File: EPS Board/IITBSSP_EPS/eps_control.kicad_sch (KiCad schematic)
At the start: 0 parts

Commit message: Started EPS Control unit design
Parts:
- added 120R: FerriteBead, symbol Device:FerriteBead
- added C10, C11, C16, C5, C6, C7, C8, C9: 100nF, symbol Device:C
- added C12: 10uF, symbol Device:C
- added C13: 10nF, symbol Device:C
- added C14, C15: 1uF, symbol Device:C
- added C17, C18: 6pF, symbol Device:C
- added J1: USB_B_Micro, symbol Connector:USB_B_Micro
- added R5: 10k, symbol Device:R
- added SW1: SW_SPDT, symbol Switch:SW_SPDT
- added U2: STM32L476VET6, Package_QFP:LQFP-100_14x14mm_P0.5mm, symbol MCU_ST_STM32L4:STM32L476VETx
- added Y1: 32MHz, symbol Device:Crystal_GND24
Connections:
- new net +3.3V: 120R.2, C10.1, C11.1, C12.1, C15.1, C5.1, C6.1, C7.1, C8.1, C9.1, SW1.3 (C), U2.100 (VDD), U2.11 (VDD), U2.22 (VDDA), U2.28 (VDD), U2.50 (VDD), U2.6 (VBAT), U2.75 (VDD)
- new net +3.3VA: 120R.1, C13.1, C14.1, U2.73 (VDDUSB)
- new net BOOT0: R5.2, U2.94 (BOOT0)
- new net GND: C10.2, C11.2, C12.2, C13.2, C14.2, C15.2, C16.2, C17.2, C18.2, C5.2, C6.2, C7.2, C8.2, C9.2, J1.5 (GND), SW1.1 (A), U2.10 (VSS), U2.19 (VSSA), U2.27 (VSS), U2.49 (VSS), U2.74 (VSS), U2.99 (VSS), Y1.2, Y1.4
- new net HSE_IN: C17.1, U2.12 (PH0), Y1.1
- new net HSE_OUT: C18.1, U2.13 (PH1), Y1.3
- new net NRST: C16.1, U2.14 (NRST)
- new net SWCLK: U2.76 (PA14)
- new net SWDIO: U2.72 (PA13)
- new net SW_BOOT0: R5.1, SW1.2 (B)
- new net USB_D+: J1.3 (D+), U2.71 (PA12)
- new net USB_D-: J1.2 (D-), U2.70 (PA11)
- new net VBUS: J1.1 (VBUS)
- no-connect marks 0 -> 2
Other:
- note added: "Crystal Circuitry"
- note added: "Load Capacitance = (8-5)*2 = 6pF [8pF (Datasheet) - Stray Capacitance (approx 5pF)]*2"
- note added: "NOTE: VBAT should be tied to external battery or RTC for now have connected with VDD"
- note added: "USB Circuitry"
- company: (none) -> IIT Bombay Student Satellite Program
- title: (none) -> EPS Control Unit

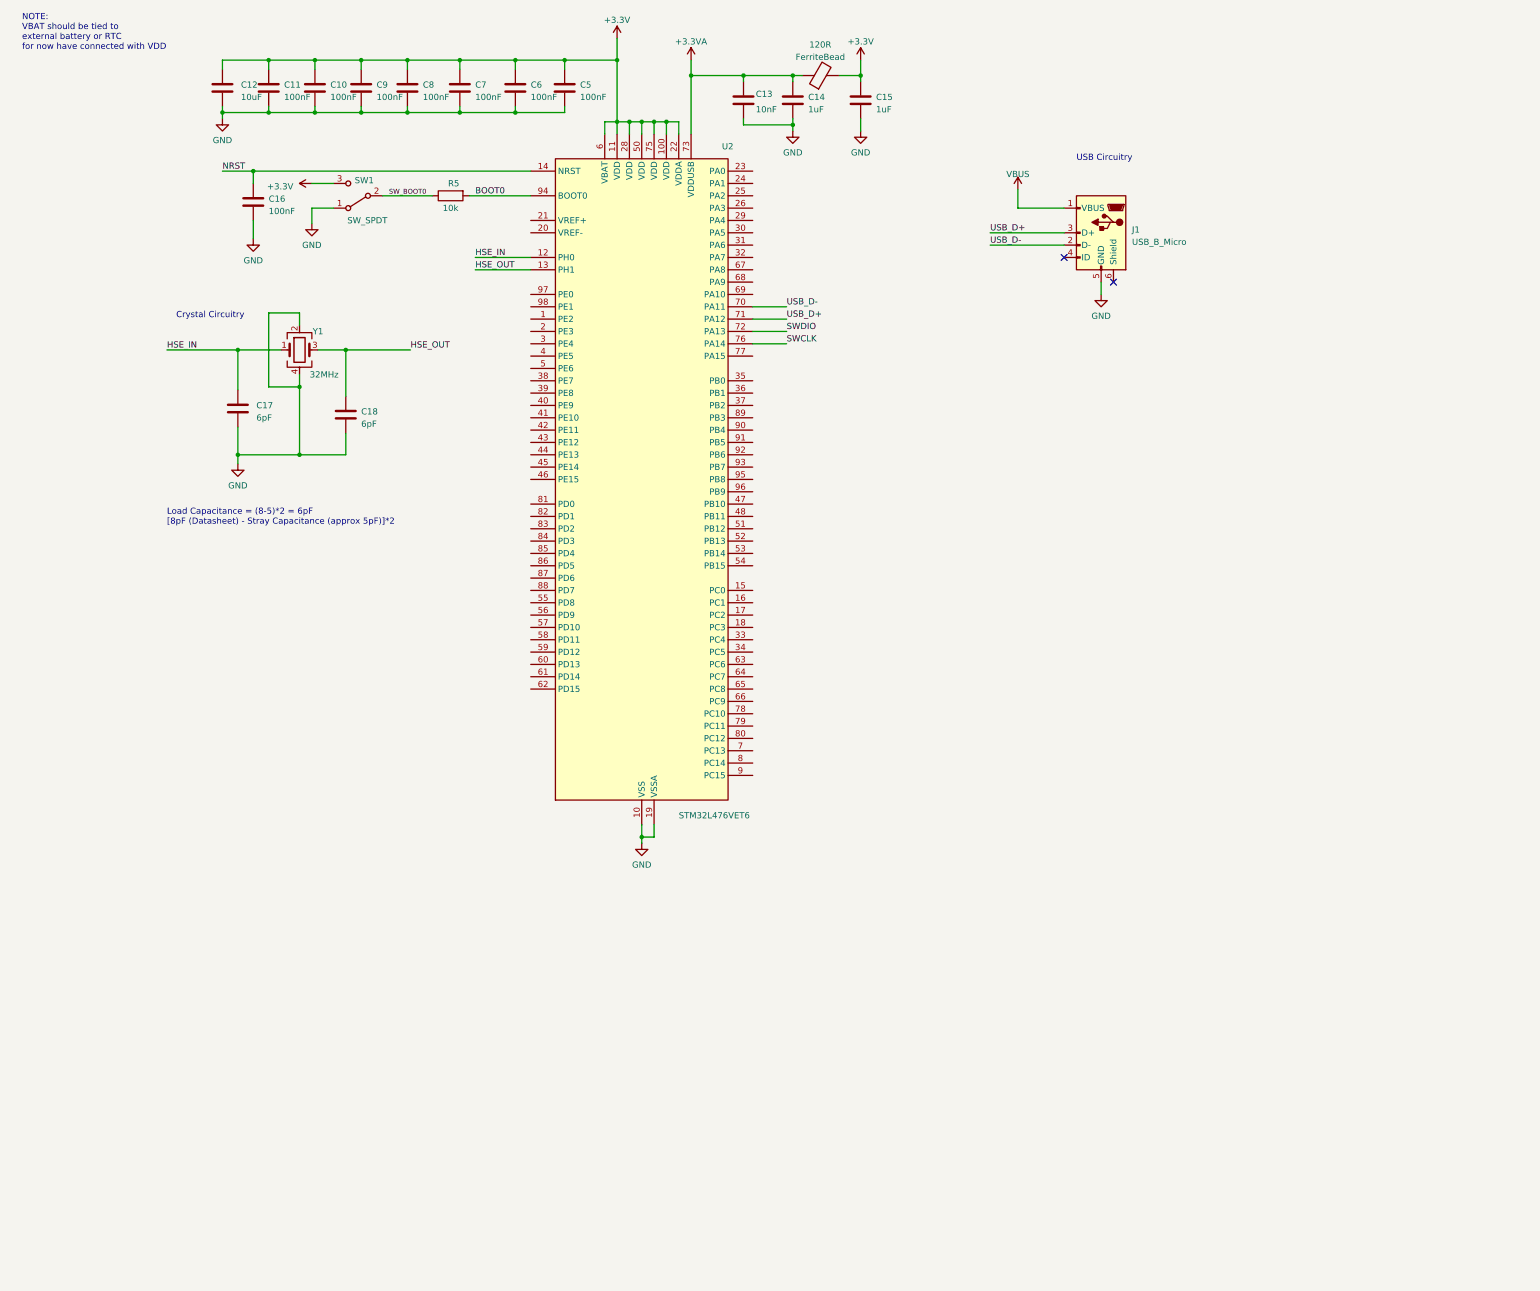
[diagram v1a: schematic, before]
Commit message: EPS Control Unit Dev and Final Schematic designed
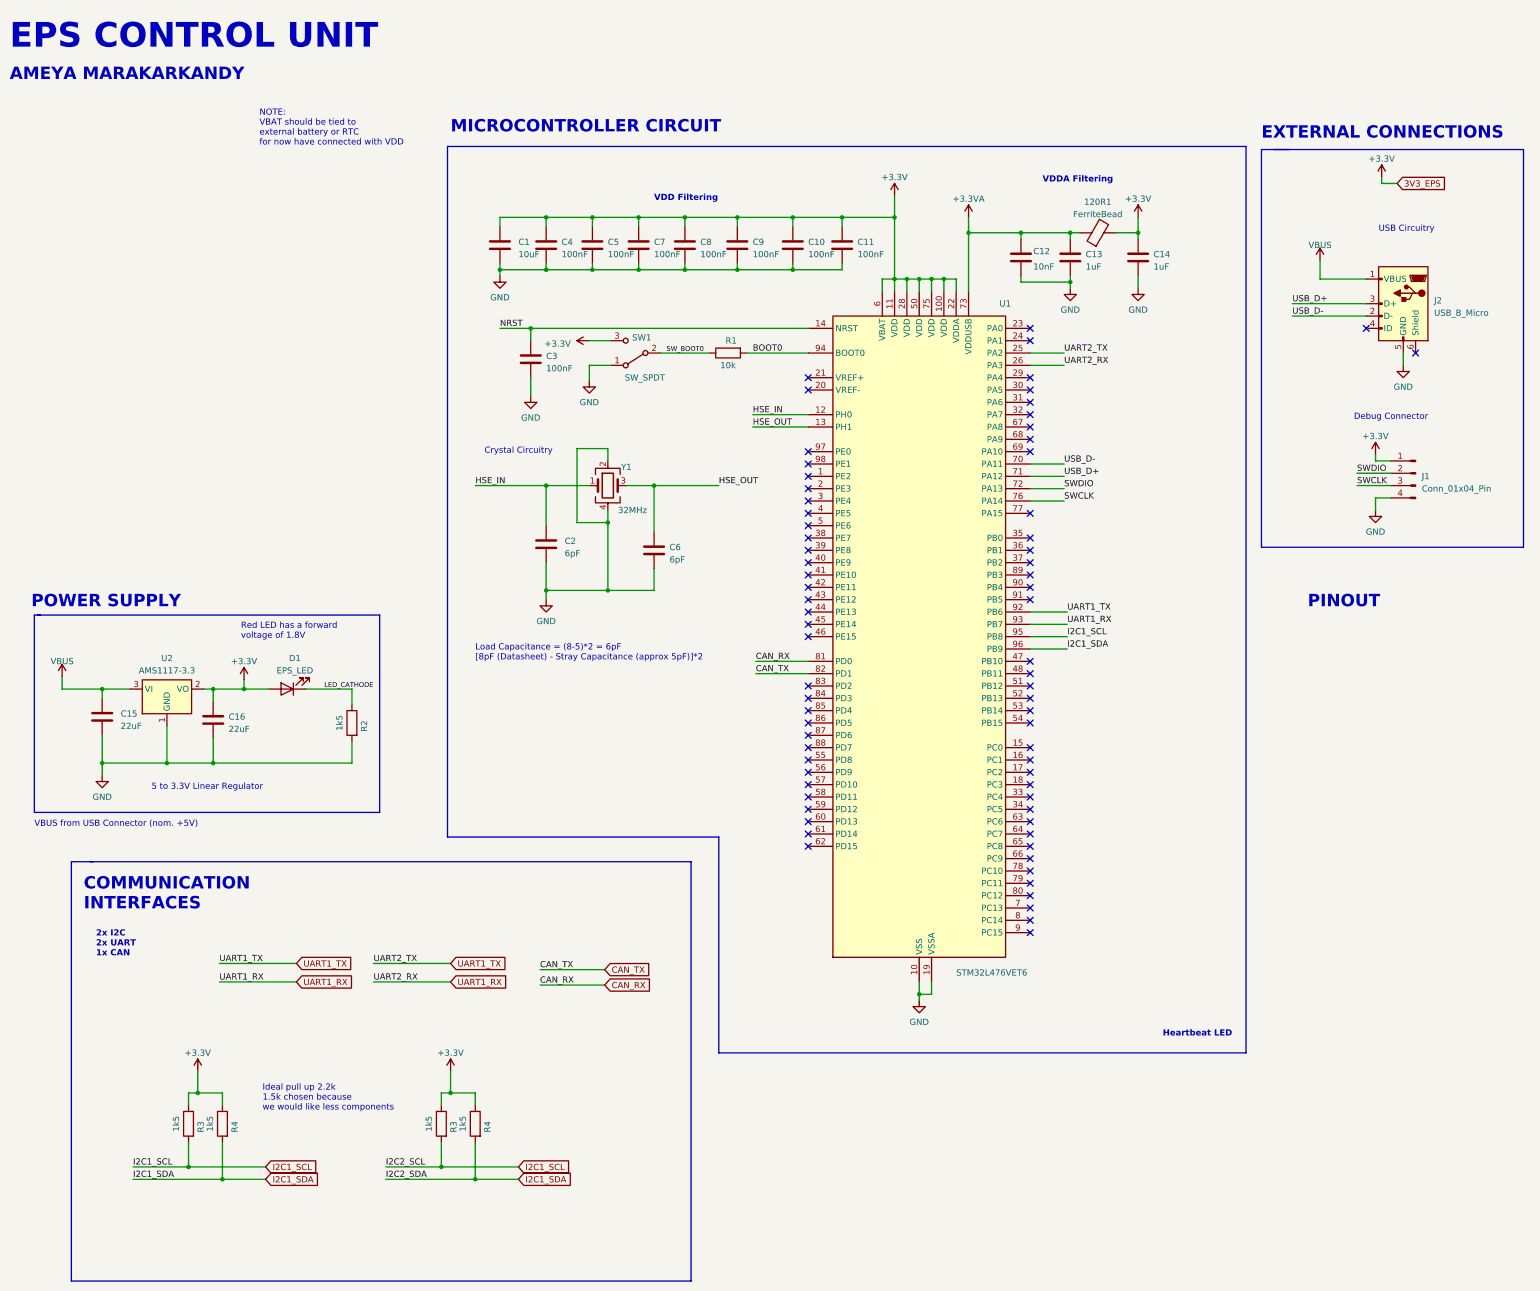
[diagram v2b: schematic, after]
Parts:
- removed 120R: FerriteBead, symbol Device:FerriteBead
- removed C17, C18: 6pF, symbol Device:C
- removed J1: USB_B_Micro, symbol Connector:USB_B_Micro
- removed R5: 10k, symbol Device:R
- removed U2: STM32L476VET6, Package_QFP:LQFP-100_14x14mm_P0.5mm, symbol MCU_ST_STM32L4:STM32L476VETx
- added 120R1: FerriteBead, symbol Device:FerriteBead
- added C1: 10uF, symbol Device:C
- added C2: 6pF, symbol Device:C
- added C3, C4: 100nF, symbol Device:C
- added D1: EPS_LED, symbol Device:LED
- added J1: Conn_01x04_Pin, symbol Connector:Conn_01x04_Pin
- added J2: USB_B_Micro, symbol Connector:USB_B_Micro
- added R1: 10k, symbol Device:R
- added R2, R3 (x2), R4 (x2): 1k5, symbol Device:R
- added U1: STM32L476VET6, Package_QFP:LQFP-100_14x14mm_P0.5mm, symbol MCU_ST_STM32L4:STM32L476VETx
- added U2: AMS1117-3.3, Package_TO_SOT_SMD:SOT-223-3_TabPin2, symbol Regulator_Linear:AMS1117-3.3
- C12: value 10uF -> 10nF
- C13: value 10nF -> 1uF
- C15: value 1uF -> 22uF
- C16: value 100nF -> 22uF
- C6: value 100nF -> 6pF
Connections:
- net +3.3V: now also C14.1, C16.1, 120R1.2, C1.1, C4.1, D1.2 (A), J1.1 (Pin_1), R3.1, R3.1, R4.1, R4.1, U1.100 (VDD), U1.11 (VDD), U1.22 (VDDA), U1.28 (VDD), U1.50 (VDD), U1.6 (VBAT), U1.75 (VDD), U2.2 (VO); no longer C12.1, C15.1, C6.1
- net +3.3VA: now also C12.1, 120R1.1, U1.73 (VDDUSB); no longer C14.1
- net BOOT0: now also R1.2, U1.94 (BOOT0)
- net GND: now also C1.2, C2.2, C3.2, C4.2, J1.4 (Pin_4), J2.5 (GND), R2.2, U1.10 (VSS), U1.19 (VSSA), U1.27 (VSS), U1.49 (VSS), U1.74 (VSS), U1.99 (VSS), U2.1 (GND)
- net HSE_IN: now also C2.1, U1.12 (PH0)
- net HSE_OUT: now also C6.1, U1.13 (PH1)
- net NRST: now also C3.1, U1.14 (NRST); no longer C16.1
- net SWCLK: now also J1.3 (Pin_3), U1.76 (PA14)
- net SWDIO: now also J1.2 (Pin_2), U1.72 (PA13)
- net SW_BOOT0: now also R1.1
- net USB_D+: now also J2.3 (D+), U1.71 (PA12)
- net USB_D-: now also J2.2 (D-), U1.70 (PA11)
- net VBUS: now also C15.1, J2.1 (VBUS), U2.3 (VI)
- new net CAN_RX: U1.81 (PD0)
- new net CAN_TX: U1.82 (PD1)
- new net I2C1_SCL: R3.2, R3.2, U1.95 (PB8)
- new net I2C1_SDA: R4.2, R4.2, U1.96 (PB9)
- new net LED_CATHODE: D1.1 (K), R2.1
- new net UART1_RX: U1.26 (PA3), U1.93 (PB7)
- new net UART1_TX: U1.25 (PA2), U1.92 (PB6)
- no-connect marks 2 -> 72
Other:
- note added: "2x I2C 2x UART 1x CAN"
- note added: "5 to 3.3V Linear Regulator"
- note added: "AMEYA MARAKARKANDY"
- note added: "COMMUNICATION INTERFACES"
- note added: "Debug Connector"
- note added: "EPS CONTROL UNIT"
- note added: "EXTERNAL CONNECTIONS"
- note added: "Heartbeat LED"
- note added: "Ideal pull up 2.2k 1.5k chosen because we would like less components"
- note added: "MICROCONTROLLER CIRCUIT"
- note added: "PINOUT"
- note added: "POWER SUPPLY"
- note added: "Red LED has a forward voltage of 1.8V"
- note added: "VBUS from USB Connector (nom. +5V)"
- note added: "VDD Filtering"
- note added: "VDDA Filtering"
